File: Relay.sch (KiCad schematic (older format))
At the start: 11 parts

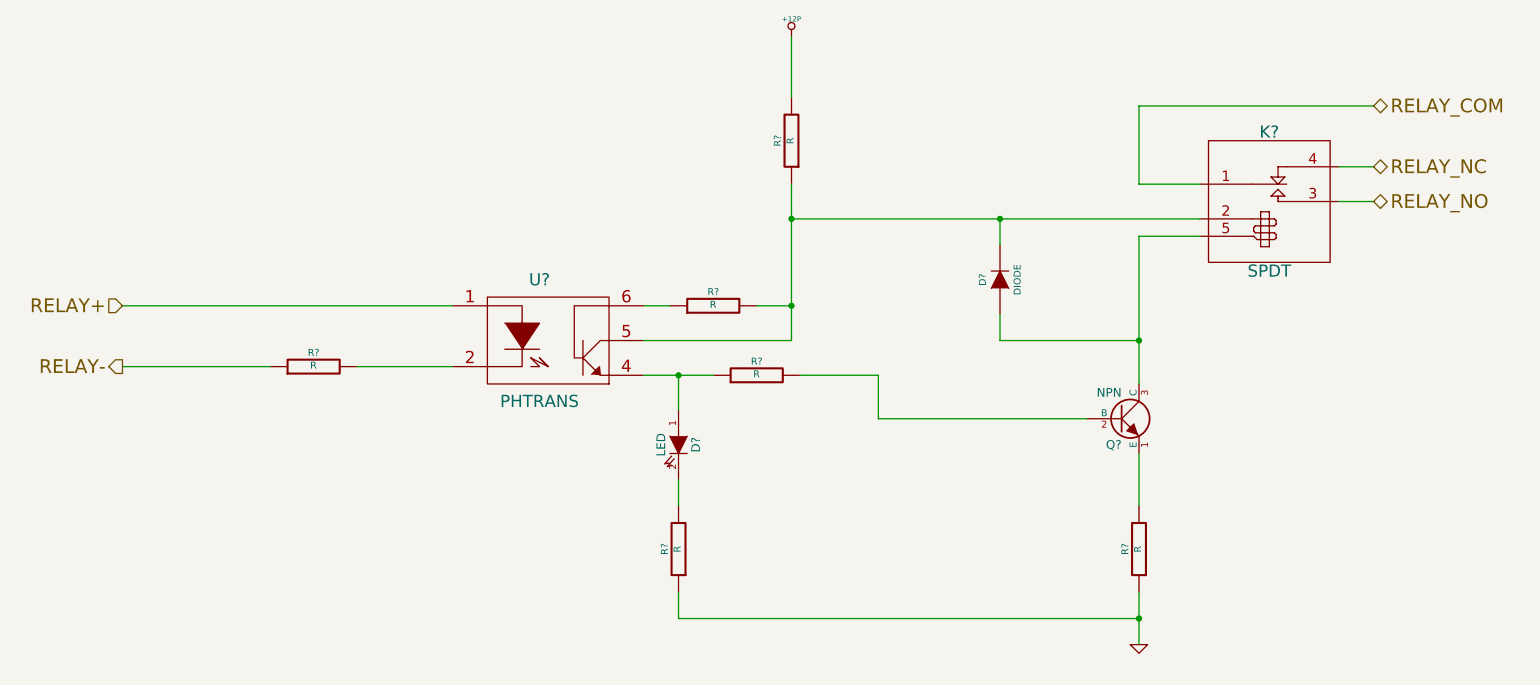
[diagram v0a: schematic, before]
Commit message: Added Relay module footprints.
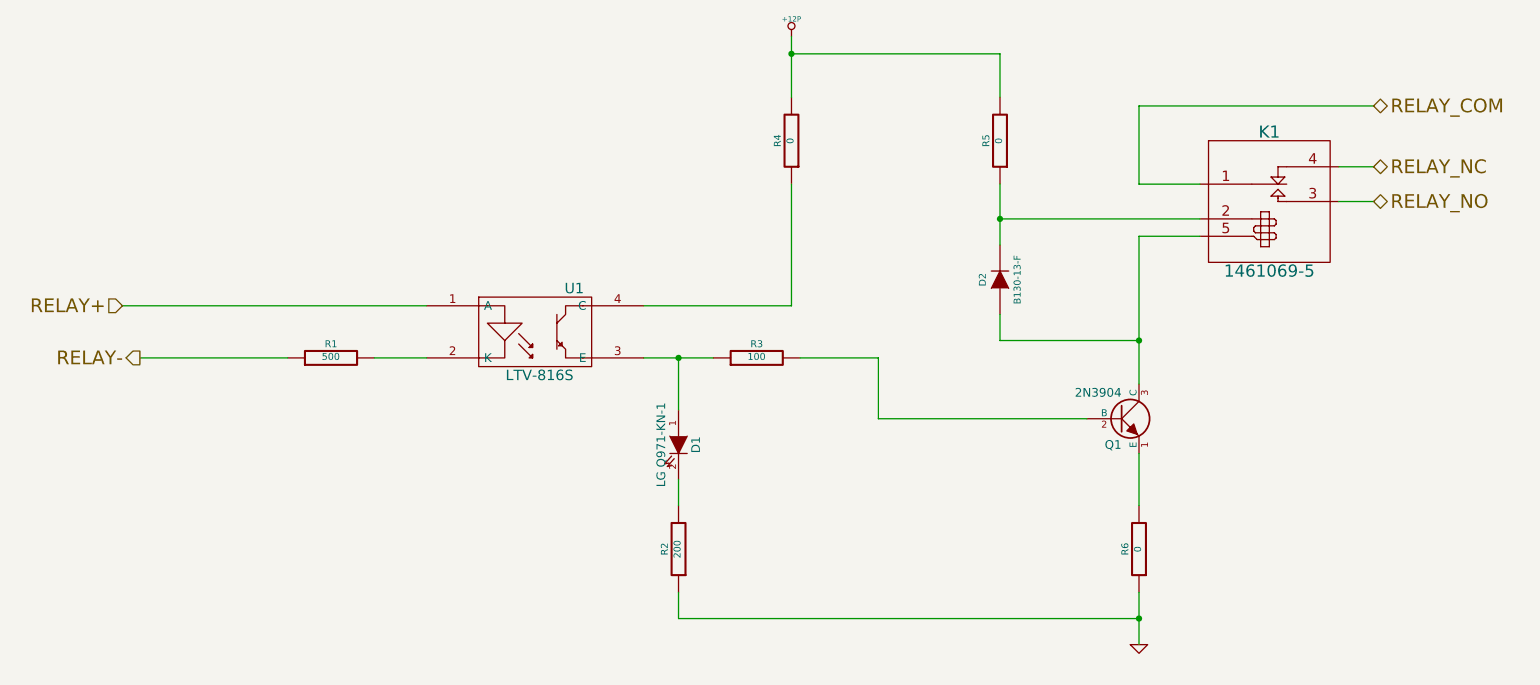
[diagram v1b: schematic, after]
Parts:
- removed R?: R, symbol R
- removed U?: PHTRANS, symbol PHTRANS
- added R5: 0, symbol R
- added U1: LTV-816S, symbol OPTO-TRANSISTOR4
- D1: renamed from D?; value LED -> LG Q971-KN-1; MFG Part Number (none) -> LG Q971-KN-1; MFG name (none) -> OSRAM Opto Semiconductors Inc
- D2: renamed from D?; value DIODE -> B130-13-F; MFG Part Number (none) -> B130-13-F; MFG name (none) -> Diodes Incorporated
- K1: renamed from K?; value SPDT -> 1461069-5; MFG Part Number (none) -> 1461069-5; MFG name (none) -> TE Connectivity
- Q1: renamed from Q?; value NPN -> 2N3904; MFG Part Number (none) -> MMBT3904-7-F; MFG name (none) -> Diodes Incorporated
- R1: renamed from R?; value R -> 500
- R2: renamed from R?; value R -> 200
- R3: renamed from R?; value R -> 100
- R4, R6: renamed from R?; value R -> 0
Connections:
- net +12P: now also R5.2
- net RELAY+: now also U1.1 (A)
- net at R1.2: now also U1.2 (K)
- net at D1.1 (A), R3.1: now also U1.3 (E)
- net at D2.2 (K), K1.2 (coil+): now also R5.1; no longer R4.1
- new net: R4.1, U1.4 (C)
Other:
- moved on the sheet: R1, R3
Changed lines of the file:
@@
 LIBS:valves
 LIBS:BB
+LIBS:GLSP
 LIBS:BB-cache
 EELAYER 24 0
@@
 $Descr A4 11693 8268
 encoding utf-8
-Sheet 8 9
+Sheet 6 9
 Title ""
 Date ""
@@
 Text HLabel 3150 2900 0    79   Input ~ 0
 RELAY+
-Text HLabel 3150 3250 0    79   Output ~ 0
+Text HLabel 3250 3200 0    79   Output ~ 0
 RELAY-
 Text HLabel 10350 2100 2    79   BiDi ~ 0
@@
 RELAY_NO
 $Comp
-L PHTRANS U?
-U 1 1 52F6443F
-P 5600 3100
-F 0 "U?" H 5550 3450 70  0000 C CNN
-F 1 "PHTRANS" H 5550 2750 70  0000 C CNN
-F 2 "" H 5600 3100 60  0000 C CNN
-F 3 "" H 5600 3100 60  0000 C CNN
-	1    5600 3100
-	1    0    0    -1
-$EndComp
-$Comp
-L NPN Q?
+L NPN Q1
 U 1 1 52F64453
 P 8900 3550
-F 0 "Q?" H 8900 3400 50  0000 R CNN
-F 1 "NPN" H 8900 3700 50  0000 R CNN
+F 0 "Q1" H 8900 3400 50  0000 R CNN
+F 1 "2N3904" H 8900 3700 50  0000 R CNN
 F 2 "" H 8900 3550 60  0000 C CNN
 F 3 "" H 8900 3550 60  0000 C CNN
+F 4 "Diodes Incorporated" H 8900 3550 60  0001 C CNN "MFG name"
+F 5 "MMBT3904-7-F " H 8900 3550 60  0001 C CNN "MFG Part Number"
 	1    8900 3550
 	1    0    0    -1
 $EndComp
 $Comp
-L LED D?
+L LED D1
 U 1 1 52F64467
 P 6350 3700
-F 0 "D?" H 6350 3800 50  0000 C CNN
-F 1 "LED" H 6350 3600 50  0000 C CNN
+F 0 "D1" H 6350 3800 50  0000 C CNN
+F 1 "LG Q971-KN-1" H 6350 3600 50  0000 C CNN
 F 2 "" H 6350 3700 60  0000 C CNN
 F 3 "" H 6350 3700 60  0000 C CNN
+F 4 "OSRAM Opto Semiconductors Inc" H 6350 3700 60  0001 C CNN "MFG name"
+F 5 "LG Q971-KN-1" H 6350 3700 60  0001 C CNN "MFG Part Number"
 	1    6350 3700
 	0    1    1    0
 $EndComp
 $Comp
-L R R?
+L R R3
 U 1 1 52F6447B
-P 6800 3300
-F 0 "R?" V 6880 3300 40  0000 C CNN
-F 1 "R" V 6807 3301 40  0000 C CNN
-F 2 "" V 6730 3300 30  0000 C CNN
-F 3 "" H 6800 3300 30  0000 C CNN
-	1    6800 3300
+P 6800 3200
+F 0 "R3" V 6880 3200 40  0000 C CNN
+F 1 "100" V 6807 3201 40  0000 C CNN
+F 2 "" V 6730 3200 30  0000 C CNN
+F 3 "" H 6800 3200 30  0000 C CNN
+	1    6800 3200
 	0    -1   -1   0
 $EndComp
 $Comp
-L SPDT K?
+L SPDT K1
 U 1 1 52F653E7
 P 9750 2300
-F 0 "K?" H 9750 2700 70  0000 C CNN
-F 1 "SPDT" H 9750 1900 70  0000 C CNN
+F 0 "K1" H 9750 2700 70  0000 C CNN
+F 1 "1461069-5" H 9750 1900 70  0000 C CNN
 F 2 "" H 9750 2450 60  0000 C CNN
 F 3 "" H 9750 2450 60  0000 C CNN
+F 4 "TE Connectivity" H 9750 2300 60  0001 C CNN "MFG name"
+F 5 "1461069-5" H 9750 2300 60  0001 C CNN "MFG Part Number"
 	1    9750 2300
 	1    0    0    -1
@@
 	9000 3750 9000 4050
 Wire Wire Line
-	6150 3300 6350 3300
-Wire Wire Line
-	6350 3300 6550 3300
-Wire Wire Line
-	7000 2200 7000 2400
-Wire Wire Line
-	7000 2400 7000 2900
-Wire Wire Line
-	7000 2900 7000 3100
-$Comp
-L R R?
+	6150 3200 6550 3200
+Wire Wire Line
+	7000 2200 7000 2900
+$Comp
+L R R6
 U 1 1 52F69182
 P 9000 4300
-F 0 "R?" V 9080 4300 40  0000 C CNN
-F 1 "R" V 9007 4301 40  0000 C CNN
+F 0 "R6" V 9080 4300 40  0000 C CNN
+F 1 "0" V 9007 4301 40  0000 C CNN
 F 2 "" V 8930 4300 30  0000 C CNN
 F 3 "" H 9000 4300 30  0000 C CNN
@@
 $EndComp
 $Comp
-L R R?
+L R R2
 U 1 1 52F6918D
 P 6350 4300
-F 0 "R?" V 6430 4300 40  0000 C CNN
-F 1 "R" V 6357 4301 40  0000 C CNN
+F 0 "R2" V 6430 4300 40  0000 C CNN
+F 1 "200" V 6357 4301 40  0000 C CNN
 F 2 "" V 6280 4300 30  0000 C CNN
 F 3 "" H 6350 4300 30  0000 C CNN
@@
 $EndComp
 Wire Wire Line
-	6350 3500 6350 3300
-Connection ~ 6350 3300
+	6350 3500 6350 3200
+Connection ~ 6350 3200
 Wire Wire Line
 	6350 4050 6350 3900
 $Comp
-L GND #PWR?
+L GND #PWR30
 U 1 1 52F691B6
 P 9000 4850
-F 0 "#PWR?" H 9000 4850 30  0001 C CNN
+F 0 "#PWR30" H 9000 4850 30  0001 C CNN
 F 1 "GND" H 9000 4780 30  0001 C CNN
 F 2 "" H 9000 4850 60  0000 C CNN
@@
 $EndComp
 Wire Wire Line
-	9000 4550 9000 4700
-Wire Wire Line
-	9000 4700 9000 4850
+	9000 4550 9000 4850
 Wire Wire Line
 	6350 4550 6350 4700
@@
 Connection ~ 9000 4700
 $Comp
-L R R?
+L R R4
 U 1 1 52F69252
 P 7000 1950
-F 0 "R?" V 7080 1950 40  0000 C CNN
-F 1 "R" V 7007 1951 40  0000 C CNN
+F 0 "R4" V 7080 1950 40  0000 C CNN
+F 1 "0" V 7007 1951 40  0000 C CNN
 F 2 "" V 6930 1950 30  0000 C CNN
 F 3 "" H 7000 1950 30  0000 C CNN
@@
 $EndComp
 $Comp
-L R R?
-U 1 1 52F6925D
-P 6550 2900
-F 0 "R?" V 6630 2900 40  0000 C CNN
-F 1 "R" V 6557 2901 40  0000 C CNN
-F 2 "" V 6480 2900 30  0000 C CNN
-F 3 "" H 6550 2900 30  0000 C CNN
-	1    6550 2900
-	0    -1   -1   0
-$EndComp
-$Comp
-L +12P #PWR?
+L +12P #PWR29
 U 1 1 52F69275
 P 7000 1350
-F 0 "#PWR?" H 7000 1320 30  0001 C CNN
+F 0 "#PWR29" H 7000 1320 30  0001 C CNN
 F 1 "+12P" H 7000 1450 30  0000 C CNN
 F 2 "" H 7000 1350 60  0000 C CNN
@@
 	7000 1700 7000 1350
 Wire Wire Line
-	7000 3100 6150 3100
-Wire Wire Line
-	6150 2900 6300 2900
-Wire Wire Line
-	6800 2900 7000 2900
-Connection ~ 7000 2900
-$Comp
-L R R?
+	7000 2900 6150 2900
+$Comp
+L R R1
 U 1 1 52F692DD
-P 4250 3250
-F 0 "R?" V 4330 3250 40  0000 C CNN
-F 1 "R" V 4257 3251 40  0000 C CNN
-F 2 "" V 4180 3250 30  0000 C CNN
-F 3 "" H 4250 3250 30  0000 C CNN
-	1    4250 3250
+P 4350 3200
+F 0 "R1" V 4430 3200 40  0000 C CNN
+F 1 "500" V 4357 3201 40  0000 C CNN
+F 2 "" V 4280 3200 30  0000 C CNN
+F 3 "" H 4350 3200 30  0000 C CNN
+	1    4350 3200
 	0    -1   -1   0
 $EndComp
 Wire Wire Line
-	5050 2900 3150 2900
-Wire Wire Line
-	5050 3250 4500 3250
-Wire Wire Line
-	4000 3250 3150 3250
+	3150 2900 4900 2900
+Wire Wire Line
+	4100 3200 3250 3200
 Wire Wire Line
 	10350 1750 9000 1750
 Wire Wire Line
 	9000 1750 9000 2200
-Wire Wire Line
-	9350 2400 8200 2400
-Wire Wire Line
-	8200 2400 7000 2400
-Connection ~ 7000 2400
-$Comp
-L DIODE D?
+$Comp
+L DIODE D2
 U 1 1 52F694B5
 P 8200 2750
-F 0 "D?" H 8200 2850 40  0000 C CNN
-F 1 "DIODE" H 8200 2650 40  0000 C CNN
+F 0 "D2" H 8200 2850 40  0000 C CNN
+F 1 "B130-13-F" H 8200 2650 40  0000 C CNN
 F 2 "" H 8200 2750 60  0000 C CNN
 F 3 "" H 8200 2750 60  0000 C CNN
+F 4 "Diodes Incorporated" H 8200 2750 60  0001 C CNN "MFG name"
+F 5 "B130-13-F" H 8200 2750 60  0001 C CNN "MFG Part Number"
 	1    8200 2750
 	0    -1   -1   0
 $EndComp
 Wire Wire Line
-	7050 3300 7500 3300
-Wire Wire Line
-	7500 3300 7500 3550
+	7050 3200 7500 3200
+Wire Wire Line
+	7500 3200 7500 3550
 Wire Wire Line
 	7500 3550 8700 3550
 Wire Wire Line
-	9000 2500 9000 3100
-Wire Wire Line
-	9000 3100 9000 3350
+	9000 2500 9000 3350
 Wire Wire Line
 	9000 3100 8200 3100
@@
 	8200 3100 8200 2950
 Wire Wire Line
-	8200 2550 8200 2400
+	8200 2200 8200 2550
 Connection ~ 8200 2400
 Wire Wire Line
 	9350 2500 9000 2500
 Connection ~ 9000 3100
+$Comp
+L OPTO-TRANSISTOR4 U1
+U 1 1 5302930B
+P 5550 3050
+F 0 "U1" H 5750 3300 60  0000 C CNN
+F 1 "LTV-816S" H 5550 2800 60  0000 C CNN
+F 2 "" H 5550 3050 60  0000 C CNN
+F 3 "" H 5550 3050 60  0000 C CNN
+F 4 "Lite-On Inc" H 5550 3050 60  0001 C CNN "MFG name"
+F 5 "LTV-816S" H 5550 3050 60  0001 C CNN "MFG Part Number"
+	1    5550 3050
+	1    0    0    -1
+$EndComp
+Wire Wire Line
+	4600 3200 4900 3200
+Wire Wire Line
+	8200 2400 9350 2400
+$Comp
+L R R5
+U 1 1 530297E7
+P 8200 1950
+F 0 "R5" V 8280 1950 40  0000 C CNN
+F 1 "0" V 8207 1951 40  0000 C CNN
+F 2 "" V 8130 1950 30  0000 C CNN
+F 3 "" H 8200 1950 30  0000 C CNN
+	1    8200 1950
+	-1   0    0    1
+$EndComp
+Wire Wire Line
+	8200 1700 8200 1450
+Wire Wire Line
+	8200 1450 7000 1450
+Connection ~ 7000 1450
 $EndSCHEMATC

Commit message: Layout sessions 1-4.
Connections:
- net RELAY_NC: now also K1.3 (no); no longer K1.4 (NC)
- net RELAY_NO: now also K1.4 (NC); no longer K1.3 (no)
- net GND renamed GND_RELAY
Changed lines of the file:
@@
 $Descr A4 11693 8268
 encoding utf-8
-Sheet 6 9
+Sheet 3 9
 Title ""
 Date ""
@@
 Text HLabel 3250 3200 0    79   Output ~ 0
 RELAY-
+Text HLabel 10350 2300 2    79   BiDi ~ 0
+RELAY_NC
 Text HLabel 10350 2100 2    79   BiDi ~ 0
-RELAY_NC
-Text HLabel 10350 2300 2    79   BiDi ~ 0
 RELAY_NO
 $Comp
@@
 Text HLabel 10350 1750 2    79   BiDi ~ 0
 RELAY_COM
-Wire Wire Line
-	9000 2200 9350 2200
-Wire Wire Line
-	10350 2100 10150 2100
-Wire Wire Line
-	10350 2300 10150 2300
-Wire Wire Line
-	9000 3750 9000 4050
-Wire Wire Line
-	6150 3200 6550 3200
-Wire Wire Line
-	7000 2200 7000 2900
 $Comp
 L R R6
@@
 	-1   0    0    1
 $EndComp
-Wire Wire Line
-	6350 3500 6350 3200
-Connection ~ 6350 3200
-Wire Wire Line
-	6350 4050 6350 3900
-$Comp
-L GND #PWR015
-U 1 1 52F691B6
-P 9000 4850
-F 0 "#PWR015" H 9000 4850 30  0001 C CNN
-F 1 "GND" H 9000 4780 30  0001 C CNN
-F 2 "" H 9000 4850 60  0000 C CNN
-F 3 "" H 9000 4850 60  0000 C CNN
-	1    9000 4850
-	1    0    0    -1
-$EndComp
-Wire Wire Line
-	9000 4550 9000 4850
-Wire Wire Line
-	6350 4550 6350 4700
-Wire Wire Line
-	6350 4700 9000 4700
-Connection ~ 9000 4700
 $Comp
 L R R4
@@
 $EndComp
 $Comp
-L +12P #PWR016
+L +12P #PWR015
 U 1 1 52F69275
 P 7000 1350
-F 0 "#PWR016" H 7000 1320 30  0001 C CNN
+F 0 "#PWR015" H 7000 1320 30  0001 C CNN
 F 1 "+12P" H 7000 1450 30  0000 C CNN
 F 2 "" H 7000 1350 60  0000 C CNN
@@
 	1    0    0    -1
 $EndComp
-Wire Wire Line
-	7000 1700 7000 1350
-Wire Wire Line
-	7000 2900 6150 2900
 $Comp
 L R R1
@@
 	0    -1   -1   0
 $EndComp
-Wire Wire Line
-	3150 2900 4900 2900
-Wire Wire Line
-	4100 3200 3250 3200
-Wire Wire Line
-	10350 1750 9000 1750
-Wire Wire Line
-	9000 1750 9000 2200
 $Comp
 L DIODE D2
@@
 	0    -1   -1   0
 $EndComp
-Wire Wire Line
-	7050 3200 7500 3200
-Wire Wire Line
-	7500 3200 7500 3550
-Wire Wire Line
-	7500 3550 8700 3550
-Wire Wire Line
-	9000 2500 9000 3350
-Wire Wire Line
-	9000 3100 8200 3100
-Wire Wire Line
-	8200 3100 8200 2950
-Wire Wire Line
-	8200 2200 8200 2550
-Connection ~ 8200 2400
-Wire Wire Line
-	9350 2500 9000 2500
-Connection ~ 9000 3100
 $Comp
 L OPTO-TRANSISTOR4 U1
@@
 	1    0    0    -1
 $EndComp
-Wire Wire Line
-	4600 3200 4900 3200
-Wire Wire Line
-	8200 2400 9350 2400
 $Comp
 L R R5
@@
 $EndComp
 Wire Wire Line
+	9000 2200 9350 2200
+Wire Wire Line
+	10350 2100 10150 2100
+Wire Wire Line
+	10350 2300 10150 2300
+Wire Wire Line
+	9000 3750 9000 4050
+Wire Wire Line
+	6150 3200 6550 3200
+Wire Wire Line
+	7000 2200 7000 2900
+Wire Wire Line
+	6350 3500 6350 3200
+Connection ~ 6350 3200
+Wire Wire Line
+	6350 4050 6350 3900
+Wire Wire Line
+	6350 4550 6350 4700
+Wire Wire Line
+	6350 4700 9000 4700
+Connection ~ 9000 4700
+Wire Wire Line
+	7000 1700 7000 1350
+Wire Wire Line
+	7000 2900 6150 2900
+Wire Wire Line
+	3150 2900 4900 2900
+Wire Wire Line
+	4100 3200 3250 3200
+Wire Wire Line
+	10350 1750 9000 1750
+Wire Wire Line
+	9000 1750 9000 2200
+Wire Wire Line
+	7050 3200 7500 3200
+Wire Wire Line
+	7500 3200 7500 3550
+Wire Wire Line
+	7500 3550 8700 3550
+Wire Wire Line
+	9000 2500 9000 3350
+Wire Wire Line
+	9000 3100 8200 3100
+Wire Wire Line
+	8200 3100 8200 2950
+Wire Wire Line
+	8200 2200 8200 2550
+Connection ~ 8200 2400
+Wire Wire Line
+	9350 2500 9000 2500
+Connection ~ 9000 3100
+Wire Wire Line
+	4600 3200 4900 3200
+Wire Wire Line
+	8200 2400 9350 2400
+Wire Wire Line
 	8200 1700 8200 1450
 Wire Wire Line
 	8200 1450 7000 1450
 Connection ~ 7000 1450
+Wire Wire Line
+	9000 4900 9000 4550
+$Comp
+L GND_RELAY #PWR016
+U 1 1 5313D9BA
+P 9000 4900
+F 0 "#PWR016" H 9000 4900 30  0001 C CNN
+F 1 "GND_RELAY" H 9000 4830 30  0000 C CNN
+F 2 "" H 9000 4900 60  0000 C CNN
+F 3 "" H 9000 4900 60  0000 C CNN
+	1    9000 4900
+	1    0    0    -1
+$EndComp
 $EndSCHEMATC
